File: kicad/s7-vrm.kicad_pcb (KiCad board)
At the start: 2 copper layers, 39.8 x 46.4 mm, 19 parts, among them J1 Conn_02x15_Row_Letter_First, SW1 SW_DIP_x03, U1 LM2596S, U2 LM2596S

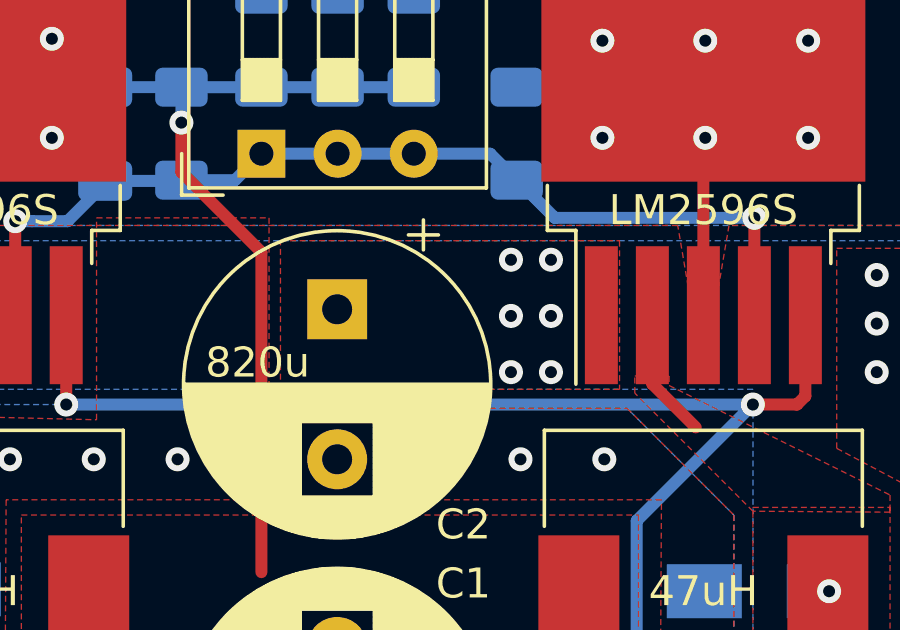
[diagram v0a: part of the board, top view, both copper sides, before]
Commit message: Renamed project into s7-vrm
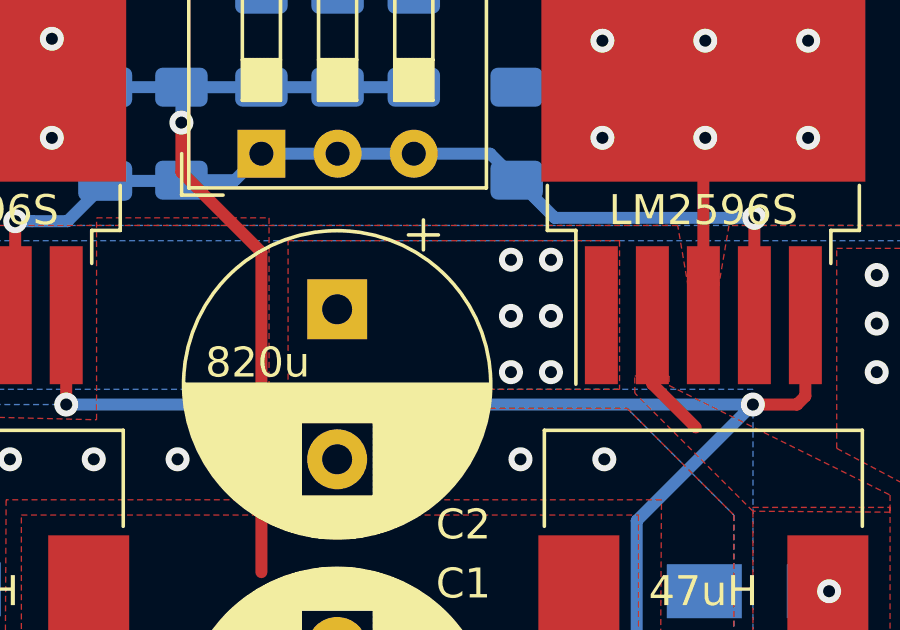
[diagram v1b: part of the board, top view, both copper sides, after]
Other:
- board text added: "S7-VRM by Necroware"
- board text removed: "MMX-VRM by Necroware"
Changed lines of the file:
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@@
   (page A4)
   (title_block
-    (title MMX-VRM)
+    (title s7-vrm)
     (date 2021-11-19)
     (rev 0.2)
@@
     (uvia_dia 0.3)
     (uvia_drill 0.1)
-    (add_net +12V)
     (add_net +3.3V)
     (add_net +5V)
@@
     (add_net "Net-(D1-Pad1)")
     (add_net "Net-(D2-Pad1)")
-    (add_net "Net-(J1-Padb11)")
     (add_net "Net-(R3-Pad2)")
     (add_net "Net-(R4-Pad2)")
@@
     (add_net SENSE)
     (add_net VCORE)
-  )
-  (module Capacitor_SMD:C_1206_3216Metric_Pad1.33x1.80mm_HandSolder (layer B.Cu)
-    (at 124.714 73.914 270)
-    (descr "Capacitor SMD 1206 (3216 Metric), square (rectangular) end terminal, IPC_7351 nominal with elongated pad for handsoldering. (Body size source: IPC-SM-782 page 76, https://www.pcb-3d.com/wordpress/wp-content/uploads/ipc-sm-782a_amendment_1_and_2.pdf), generated with kicad-footprint-generator")
-    (tags "capacitor handsolder")
-    (attr smd)
-    (fp_text reference C3 (at -3.302 0.127 180) (layer B.SilkS)
-      (effects (font (size 1 1) (thickness 0.15)) (justify mirror))
-    )
-    (fp_text value 10nF (at 0 -1.85 270) (layer B.Fab)
-      (effects (font (size 1 1) (thickness 0.15)) (justify mirror))
-    )
-    (fp_line (start -1.6 -0.8) (end -1.6 0.8) (layer B.Fab) (width 0.1))
-    (fp_line (start -1.6 0.8) (end 1.6 0.8) (layer B.Fab) (width 0.1))
-    (fp_line (start 1.6 0.8) (end 1.6 -0.8) (layer B.Fab) (width 0.1))
-    (fp_line (start 1.6 -0.8) (end -1.6 -0.8) (layer B.Fab) (width 0.1))
-    (fp_line (start -0.711252 0.91) (end 0.711252 0.91) (layer B.SilkS) (width 0.12))
-    (fp_line (start -0.711252 -0.91) (end 0.711252 -0.91) (layer B.SilkS) (width 0.12))
-    (fp_line (start -2.48 -1.15) (end -2.48 1.15) (layer B.CrtYd) (width 0.05))
-    (fp_line (start -2.48 1.15) (end 2.48 1.15) (layer B.CrtYd) (width 0.05))
-    (fp_line (start 2.48 1.15) (end 2.48 -1.15) (layer B.CrtYd) (width 0.05))
-    (fp_line (start 2.48 -1.15) (end -2.48 -1.15) (layer B.CrtYd) (width 0.05))
-    (fp_text user %R (at 0 0 270) (layer B.Fab)
-      (effects (font (size 0.8 0.8) (thickness 0.12)) (justify mirror))
-    )
-    (pad 2 smd roundrect (at 1.5625 0 270) (size 1.325 1.8) (layers B.Cu B.Paste B.Mask) (roundrect_rratio 0.188679)
-      (net 11 FB))
-    (pad 1 smd roundrect (at -1.5625 0 270) (size 1.325 1.8) (layers B.Cu B.Paste B.Mask) (roundrect_rratio 0.188679)
-      (net 3 VCORE))
-    (model ${KISYS3DMOD}/Capacitor_SMD.3dshapes/C_1206_3216Metric.wrl
-      (at (xyz 0 0 0))
-      (scale (xyz 1 1 1))
-      (rotate (xyz 0 0 0))
-    )
   )
   (module mmx-vrm:EDGE_30-pin (layer F.Cu)
@@
     (pad a1 smd rect (at 0 2.54) (size 1.27 5) (layers F.Cu F.Paste F.Mask)
       (net 1 GND))
+  )
+  (module Capacitor_SMD:C_1206_3216Metric_Pad1.33x1.80mm_HandSolder (layer B.Cu)
+    (at 124.714 73.914 270)
+    (descr "Capacitor SMD 1206 (3216 Metric), square (rectangular) end terminal, IPC_7351 nominal with elongated pad for handsoldering. (Body size source: IPC-SM-782 page 76, https://www.pcb-3d.com/wordpress/wp-content/uploads/ipc-sm-782a_amendment_1_and_2.pdf), generated with kicad-footprint-generator")
+    (tags "capacitor handsolder")
+    (attr smd)
+    (fp_text reference C3 (at -3.302 0.127 180) (layer B.SilkS)
+      (effects (font (size 1 1) (thickness 0.15)) (justify mirror))
+    )
+    (fp_text value 10nF (at 0 -1.85 270) (layer B.Fab)
+      (effects (font (size 1 1) (thickness 0.15)) (justify mirror))
+    )
+    (fp_line (start -1.6 -0.8) (end -1.6 0.8) (layer B.Fab) (width 0.1))
+    (fp_line (start -1.6 0.8) (end 1.6 0.8) (layer B.Fab) (width 0.1))
+    (fp_line (start 1.6 0.8) (end 1.6 -0.8) (layer B.Fab) (width 0.1))
+    (fp_line (start 1.6 -0.8) (end -1.6 -0.8) (layer B.Fab) (width 0.1))
+    (fp_line (start -0.711252 0.91) (end 0.711252 0.91) (layer B.SilkS) (width 0.12))
+    (fp_line (start -0.711252 -0.91) (end 0.711252 -0.91) (layer B.SilkS) (width 0.12))
+    (fp_line (start -2.48 -1.15) (end -2.48 1.15) (layer B.CrtYd) (width 0.05))
+    (fp_line (start -2.48 1.15) (end 2.48 1.15) (layer B.CrtYd) (width 0.05))
+    (fp_line (start 2.48 1.15) (end 2.48 -1.15) (layer B.CrtYd) (width 0.05))
+    (fp_line (start 2.48 -1.15) (end -2.48 -1.15) (layer B.CrtYd) (width 0.05))
+    (fp_text user %R (at 0 0 270) (layer B.Fab)
+      (effects (font (size 0.8 0.8) (thickness 0.12)) (justify mirror))
+    )
+    (pad 2 smd roundrect (at 1.5625 0 270) (size 1.325 1.8) (layers B.Cu B.Paste B.Mask) (roundrect_rratio 0.188679)
+      (net 11 FB))
+    (pad 1 smd roundrect (at -1.5625 0 270) (size 1.325 1.8) (layers B.Cu B.Paste B.Mask) (roundrect_rratio 0.188679)
+      (net 3 VCORE))
+    (model ${KISYS3DMOD}/Capacitor_SMD.3dshapes/C_1206_3216Metric.wrl
+      (at (xyz 0 0 0))
+      (scale (xyz 1 1 1))
+      (rotate (xyz 0 0 0))
+    )
   )
   (module Resistor_SMD:R_1206_3216Metric_Pad1.30x1.75mm_HandSolder (layer F.Cu)
@@
     (effects (font (size 1 1) (thickness 0.15)))
   )
-  (gr_text "MMX-VRM by Necroware" (at 132.715 61.595) (layer F.Mask)
+  (gr_text "S7-VRM by Necroware" (at 132.715 61.595) (layer F.Mask)
     (effects (font (size 2 2) (thickness 0.4)))
   )
@@
   (segment (start 127.253 72.3515) (end 127.254 72.3525) (width 0.4) (layer B.Cu) (net 3))
   (segment (start 124.714 72.3515) (end 127.253 72.3515) (width 0.4) (layer B.Cu) (net 3))
+  (segment (start 129.921 88.519) (end 129.921 77.851) (width 0.4) (layer F.Cu) (net 3))
   (segment (start 127.254 75.184) (end 127.254 73.533004) (width 0.4) (layer F.Cu) (net 3))
   (segment (start 129.921 77.851) (end 127.254 75.184) (width 0.4) (layer F.Cu) (net 3))
-  (segment (start 129.921 88.519) (end 129.921 77.851) (width 0.4) (layer F.Cu) (net 3))
   (segment (start 148.053 82.6525) (end 147.7745 82.931) (width 0.4) (layer F.Cu) (net 4))
   (segment (start 147.7745 82.931) (end 146.304 82.931) (width 0.4) (layer F.Cu) (net 4))
@@
     (polygon
       (pts
-        (xy 141.859 82.423) (xy 130.556 82.423) (xy 130.556 77.47) (xy 141.859 77.47)
+        (xy 141.859 82.423) (xy 130.81 82.423) (xy 130.81 77.47) (xy 141.859 77.47)
       )
     )

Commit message: Minor layout improvements
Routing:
- net GND: track 24.4 -> 27.1 mm, vias 35 -> 34
- net VCORE: vias 6 -> 7

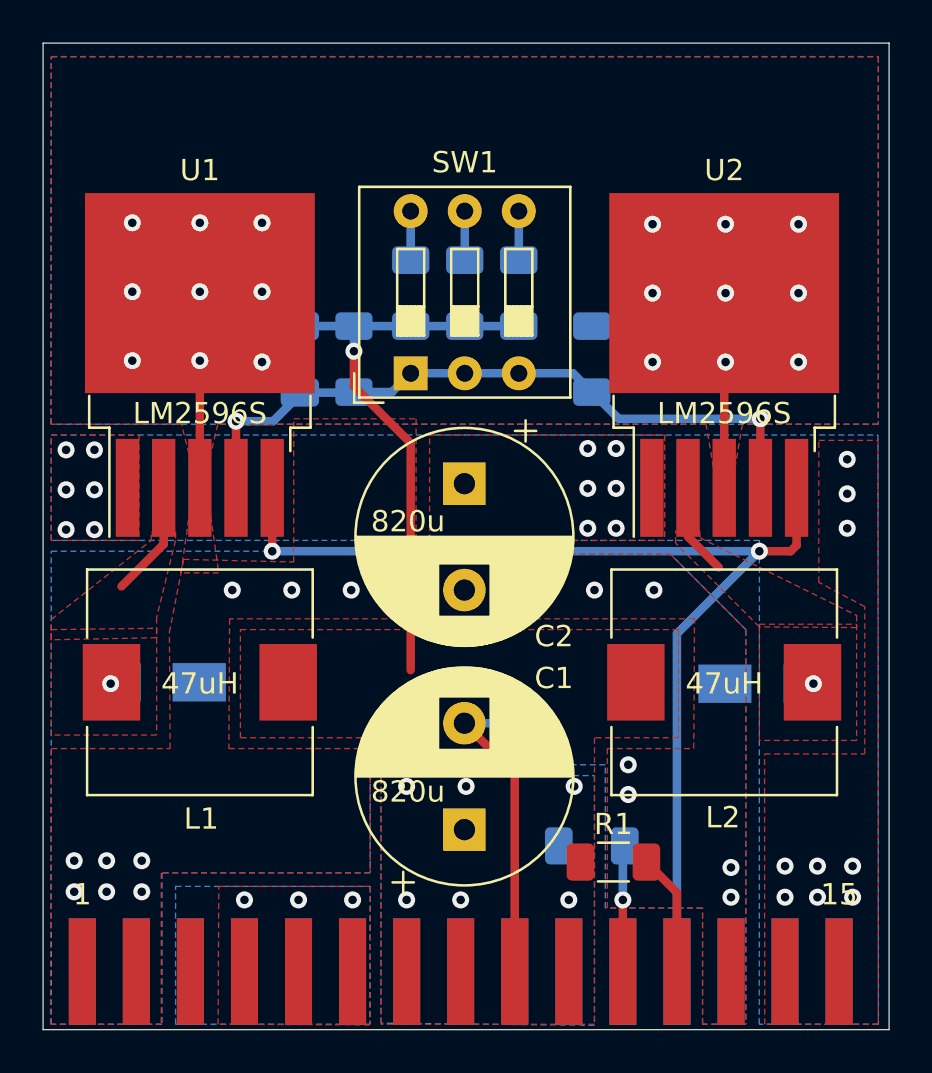
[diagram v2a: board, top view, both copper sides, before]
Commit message: Minor layout improvements
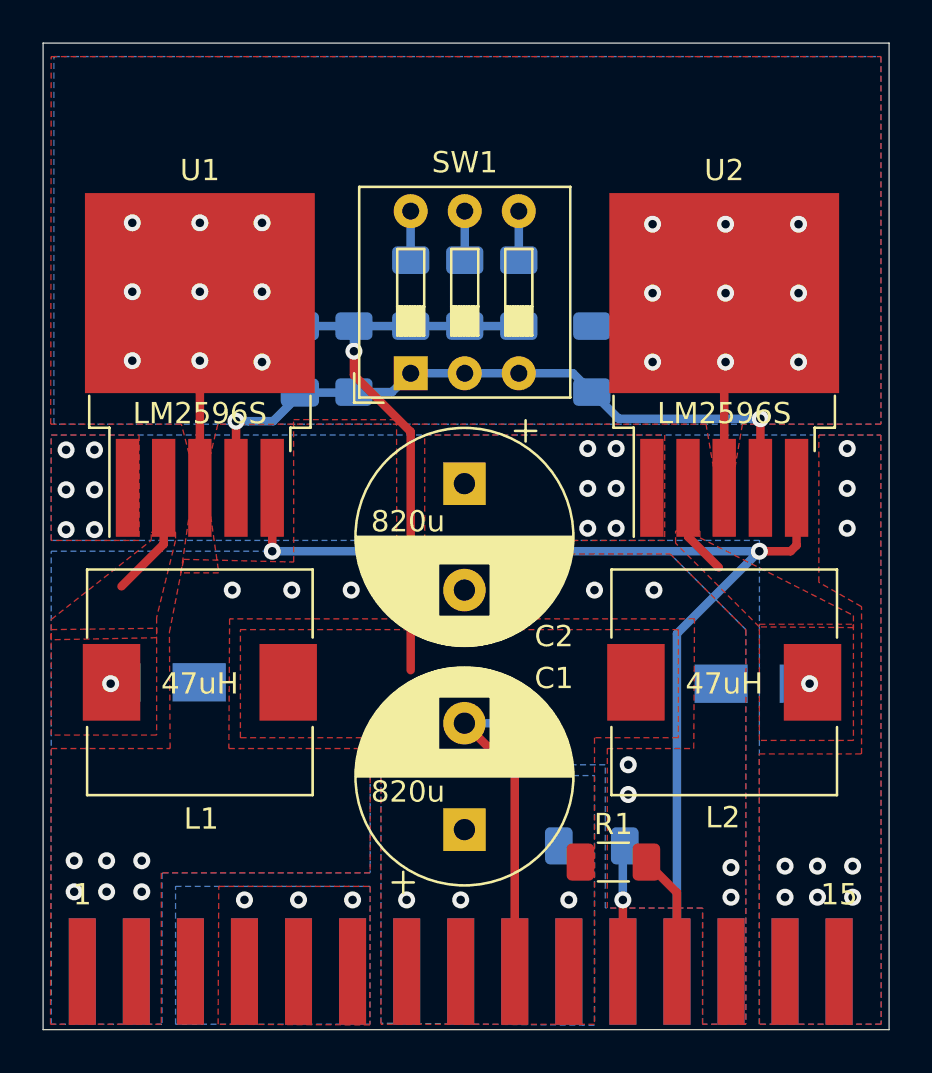
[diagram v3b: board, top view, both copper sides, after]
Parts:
- moved D2 0.18 mm to (146.5, 89.2)
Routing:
- net VCORE: vias 7 -> 4
